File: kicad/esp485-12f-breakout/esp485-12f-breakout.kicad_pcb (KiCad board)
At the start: 2 copper layers, 25.4 x 25.4 mm, 19 parts, among them J1 Conn_01x08, J2 Conn_01x08, U1 MAX3485, U2 ESP-12F, U3 AMS1117-3.3

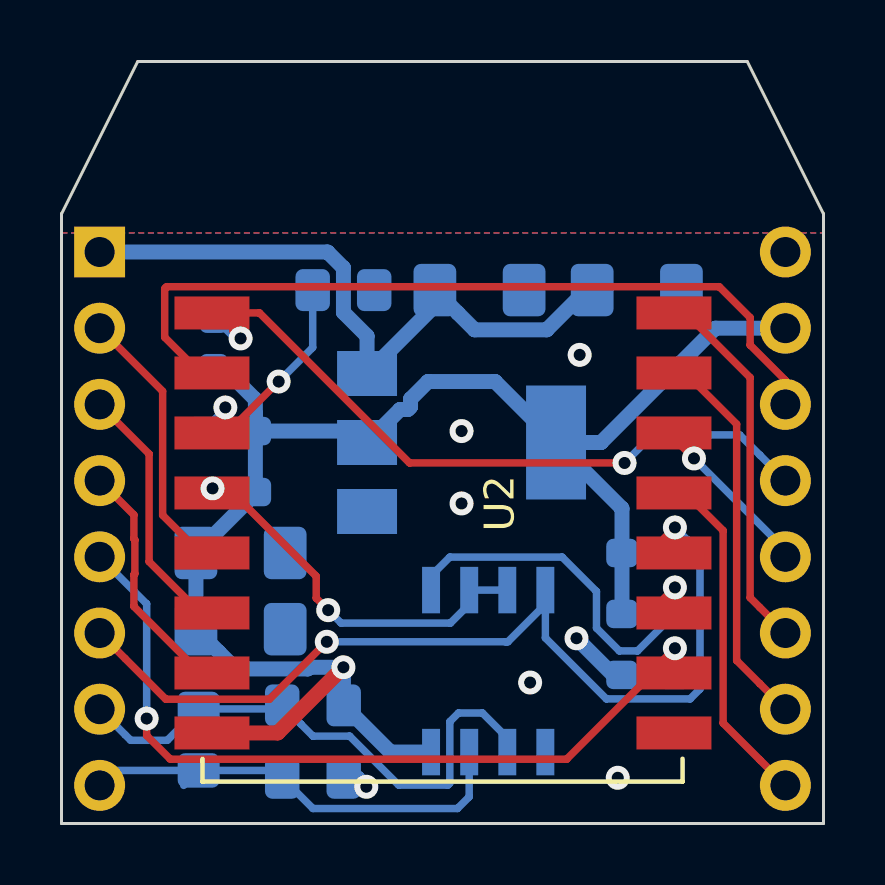
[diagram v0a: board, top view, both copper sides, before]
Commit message: migrated to single wire half duplex method
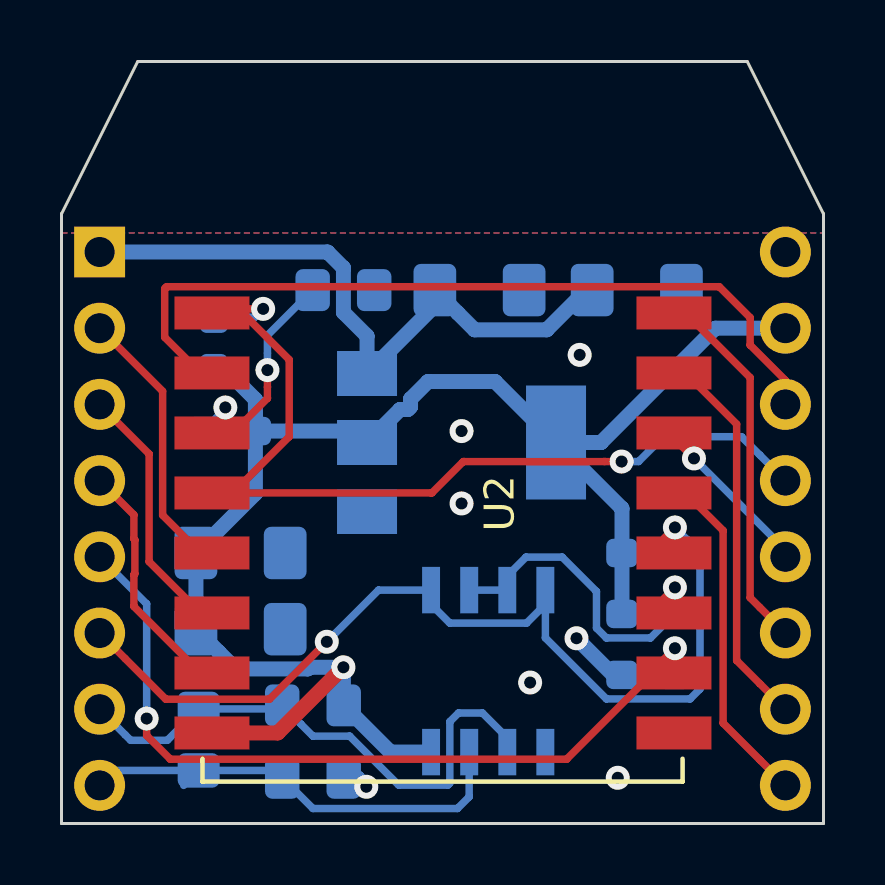
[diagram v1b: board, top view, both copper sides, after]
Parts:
- removed R8: 10K, Resistor_SMD:R_0603_1608Metric_Pad1.05x0.95mm_HandSolder
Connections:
- U1 pad 1: /IO2 -> /IO0
- U1 pad 2: /IO16 -> /IO2
- U1 pad 3: /IO16 -> /IO2
- U2 pad 4: /IO16 -> /RST
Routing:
- net /IO16: track 13.2 -> 0.00 mm, vias 2 -> 0
- net /RST: track 23.6 -> 30.4 mm
- net /IO2: track 13.4 -> 11.8 mm
- net /IO0: track 33.0 -> 34.2 mm

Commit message: added 4 layers pcb
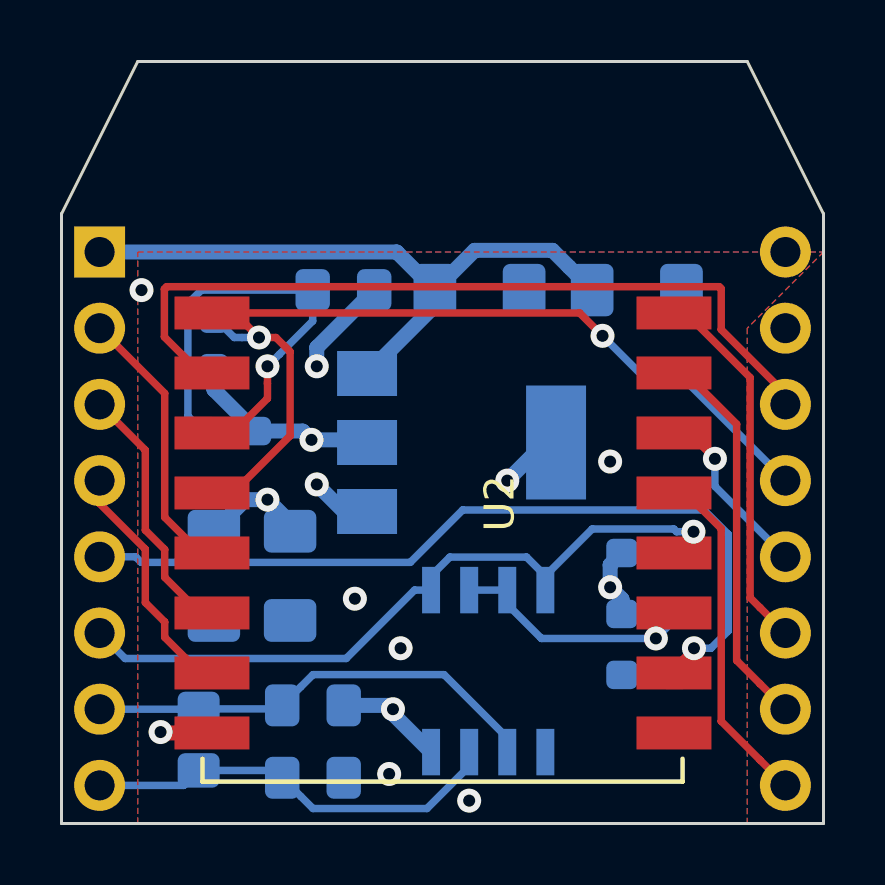
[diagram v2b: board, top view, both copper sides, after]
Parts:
- moved C4 1.99 mm to (133.3, 107.3), turned to 270 degrees
- moved C3 1.82 mm to (135.9, 107.3), turned to 270 degrees
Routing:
- net +3V3: track 53.0 -> 20.7 mm, vias 1 -> 6
- net /IO0: track 34.2 -> 25.9 mm, vias 2 -> 1
- net /EN: track 8.60 -> 14.7 mm, vias 2 -> 1
- net /A: track 18.6 -> 15.4 mm
- net /IO2: track 11.8 -> 9.13 mm
- net /IO15: track 27.0 -> 29.6 mm, vias 2 -> 1
- net GND: track 2.90 -> 5.38 mm, vias 7 -> 8
- net /B: track 15.4 -> 14.1 mm
- net /RXD: track 13.7 -> 12.6 mm
- added copper zone on In1.Cu, net +3V3
- added copper zone on In2.Cu, net GND
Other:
- copper layers 2 -> 4

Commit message: ESP-12F breakout board bump
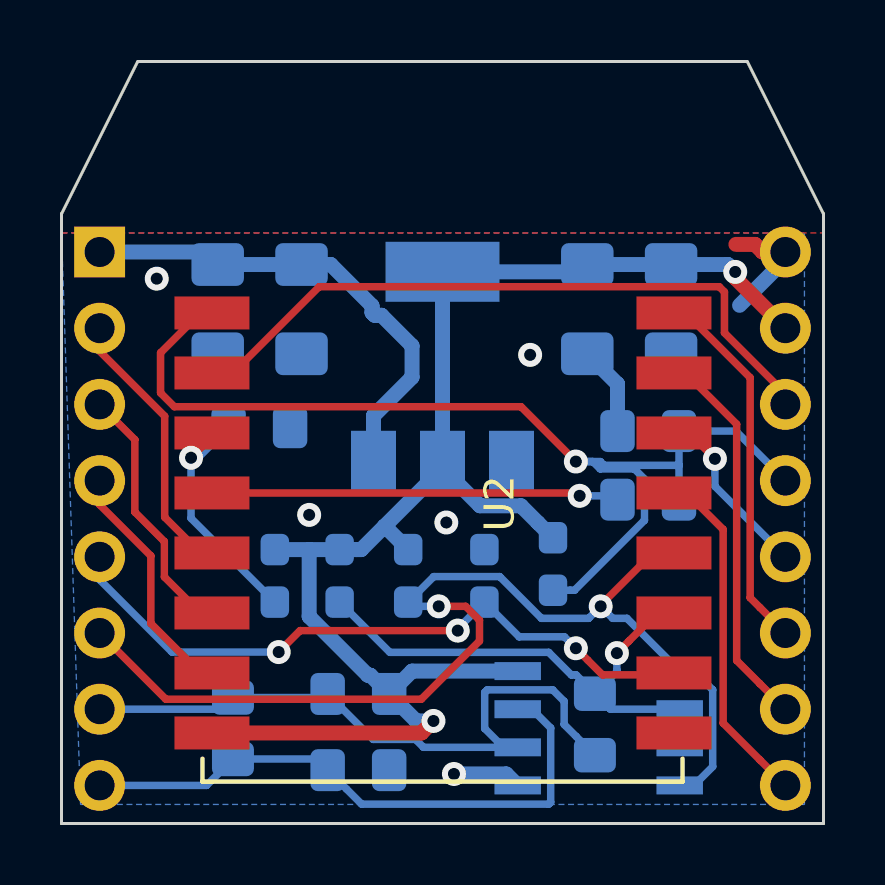
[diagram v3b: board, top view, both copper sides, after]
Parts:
- added C6: 0.1uF, Capacitor_SMD:C_0805_2012Metric_Pad1.15x1.40mm_HandSolder, B.Cu at (147.8, 102.5)
- added R6: 1k, Resistor_SMD:R_0805_2012Metric_Pad1.15x1.40mm_HandSolder, B.Cu at (147.8, 104.8)
- added R8: 0, Resistor_SMD:R_0805_2012Metric_Pad1.15x1.40mm_HandSolder, B.Cu at (146.1, 112.3)
- moved C3 15.5 mm to (148.6, 98.4)
- moved C4 15.3 mm to (145.8, 98.4)
- moved C2 14.0 mm to (133.5, 98.4), turned to 270 degrees
- moved R7 13.5 mm to (144.7, 106.9), turned to 270 degrees
- moved R2 10.4 mm to (137.5, 107.3), turned to 270 degrees
- moved R3 8.04 mm to (139.8, 107.3), turned to 270 degrees
- moved R9 6.38 mm to (142.4, 107.3), turned to 90 degrees
- moved C1 5.97 mm to (136.3, 98.4), turned to 270 degrees
- moved C5 5.36 mm to (134.9, 102.4)
- moved R1 5.06 mm to (135.4, 107.3), turned to 90 degrees
- moved U1 4.15 mm to (146.2, 112.4), turned to 180 degrees
- moved U3 2.62 mm to (141.0, 100.3), turned to 90 degrees
- moved R4 1.56 mm to (138.2, 111.3)
- moved R5 1.54 mm to (138.2, 113.8)
- moved R10 1.20 mm to (134.0, 112.4)
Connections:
- U2 pad 4: /RST -> Net-(R6-Pad1)
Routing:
- net +3V3: track 20.7 -> 51.2 mm, vias 6 -> 2
- net Net-(R6-Pad1): track 0.00 -> 12.9 mm, vias 0 -> 1
- net /IO0: track 25.9 -> 36.5 mm, vias 1 -> 2
- net /IO2: track 9.13 -> 17.6 mm
- net /IO15: track 29.6 -> 22.0 mm, vias 1 -> 3
- net /A: track 15.4 -> 22.5 mm
- net /RST: track 30.5 -> 37.0 mm, vias 2 -> 1
- net /B: track 14.1 -> 19.9 mm
- net VCC: track 21.8 -> 16.2 mm
- net /TOUT: track 27.7 -> 22.2 mm
- net /EN: track 14.7 -> 9.38 mm
- net GND: track 5.38 -> 9.44 mm, vias 8 -> 5
- net /RXD: track 12.6 -> 13.7 mm
- removed copper zone on In1.Cu, net +3V3
- removed copper zone on In2.Cu, net GND
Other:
- copper layers 4 -> 2
- board text added: "A/IO2"
- board text removed: "A"
